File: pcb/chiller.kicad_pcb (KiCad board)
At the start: 2 copper layers, 94 x 52 mm, 43 parts, among them J1 Conn_01x03, J10 Current Sense, J11 Conn_01x14, J12 Debug, J13 Conn_01x04, J2 Conn_01x03, J3 Ext, J4 Conn_01x02, J5 Conn_01x02, J6 Conn_01x02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

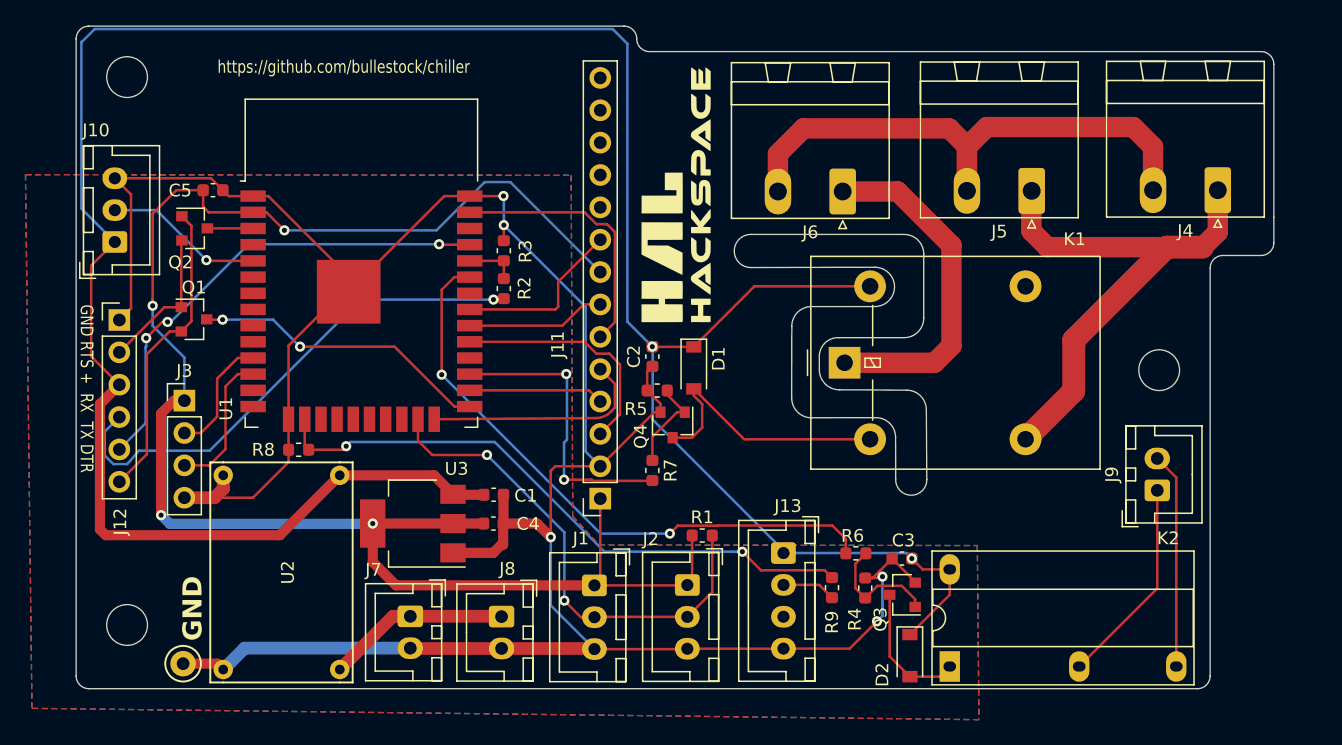
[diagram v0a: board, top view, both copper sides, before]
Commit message: Add diodes.
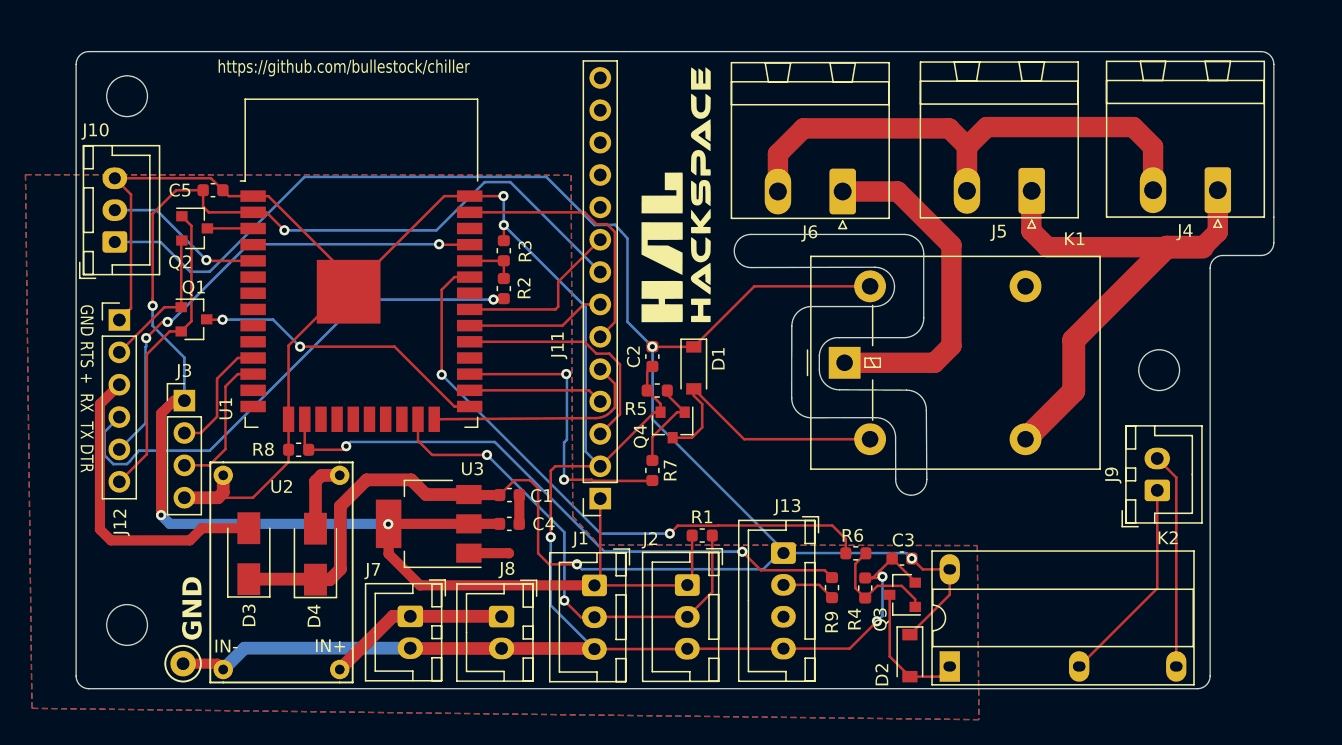
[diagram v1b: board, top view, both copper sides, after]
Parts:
- added D3: MBRA210LT3, Diode_SMD:D_SMA, F.Cu at (98.6, 114.4)
- added D4: MBRA210LT3, Diode_SMD:D_SMA, F.Cu at (103.8, 114.4)
- C1: value 1uF -> 1u
- C4: value 10uF -> 10u
- C5: value C -> 100n
- moved H1 1.50 mm to (89.0, 78.5)
- moved C4 1.24 mm to (119.0, 112.1)
- moved U3 1.24 mm to (112.7, 112.1)
- moved C1 1.24 mm to (119.0, 109.8)
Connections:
- J12 pad 3: +5V -> Net-(D3-A)
- U2 pad OUT+: +5V -> Net-(D4-A)
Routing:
- net +5V: track 202.4 -> 170.7 mm, vias 2 -> 3
- net Net-(D3-A): track 0.00 -> 24.4 mm
- net GND: track 214.1 -> 204.8 mm
- net Net-(D4-A): track 0.00 -> 5.81 mm
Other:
- board size 94 x 52 mm -> 94 x 50 mm
- board text added: "IN+"
- board text added: "IN-"

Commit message: Start adding forgotten features.
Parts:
- added J14: Flow sensor, Connector_JST:JST_XH_B3B-XH-A_1x03_P2.50mm_Vertical, F.Cu at (96.1, 78.2)
- added J15: Fan, Connector_JST:JST_XH_B2B-XH-A_1x02_P2.50mm_Vertical, F.Cu at (112.4, 78.5)
- added Q5: BSS138, Package_TO_SOT_SMD:SOT-23, F.Cu at (125.0, 79.4)
- added R10: 1k2, Resistor_SMD:R_0603_1608Metric, F.Cu at (97.9, 83.0)
- added R11: 2k2, Resistor_SMD:R_0603_1608Metric, F.Cu at (101.1, 83.0)
- J11: value Conn_01x14 -> Display; footprint Connector_PinSocket_2.54mm:PinSocket_1x14_P2.54mm_Vertical -> Connector_PinSocket_2.54mm:PinSocket_1x09_P2.54mm_Vertical
- U1: footprint RF_Module:ESP32-WROOM-32 -> RF_Module:ESP32-WROOM-32U
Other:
- board text added: "CS"
- board text added: "Fan"
- board text added: "Flow"

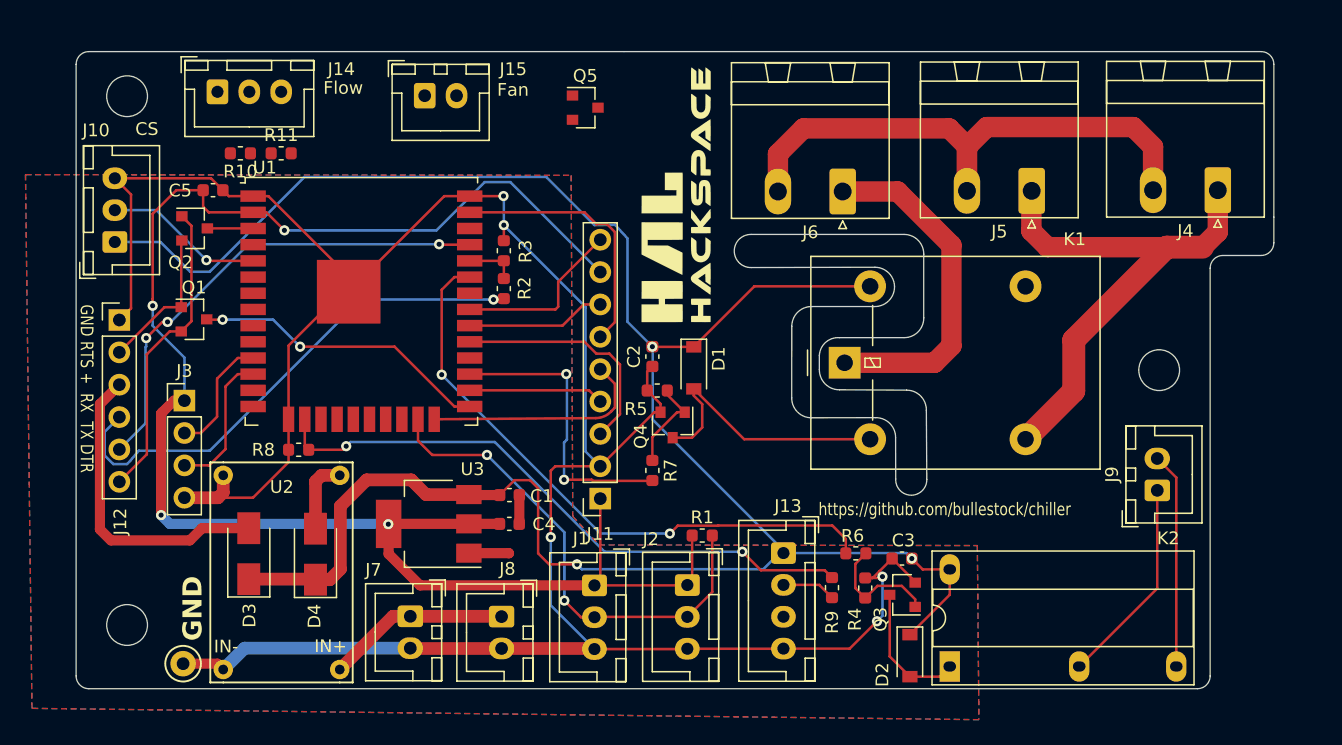
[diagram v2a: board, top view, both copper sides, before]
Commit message: Add LEDs.
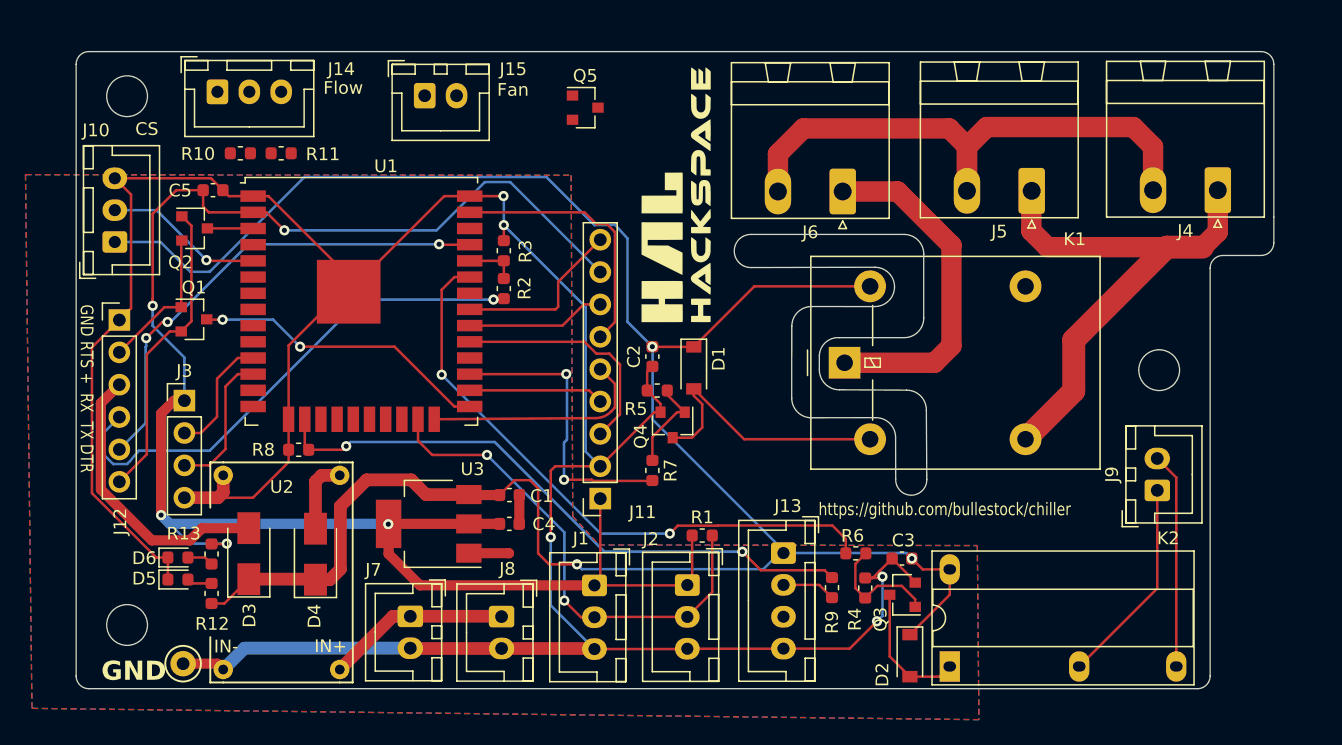
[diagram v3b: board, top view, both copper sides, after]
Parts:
- added D5: LED, LED_SMD:LED_0603_1608Metric, F.Cu at (93.0, 116.4)
- added D6: LED, LED_SMD:LED_0603_1608Metric, F.Cu at (93.0, 114.7)
- added R12: 2k7, Resistor_SMD:R_0603_1608Metric, F.Cu at (95.6, 117.5)
- added R13: 1k5, Resistor_SMD:R_0603_1608Metric, F.Cu at (95.6, 114.4)
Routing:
- net GND: track 204.8 -> 229.1 mm
- net +3V3: track 133.1 -> 140.3 mm, vias 4 -> 5
- net +5V: track 170.7 -> 174.4 mm
- net Net-(D6-A): track 0.00 -> 2.06 mm
- net Net-(D5-A): track 0.00 -> 1.98 mm
- net Net-(D3-A): track 24.4 -> 22.5 mm

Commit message: Move J9.
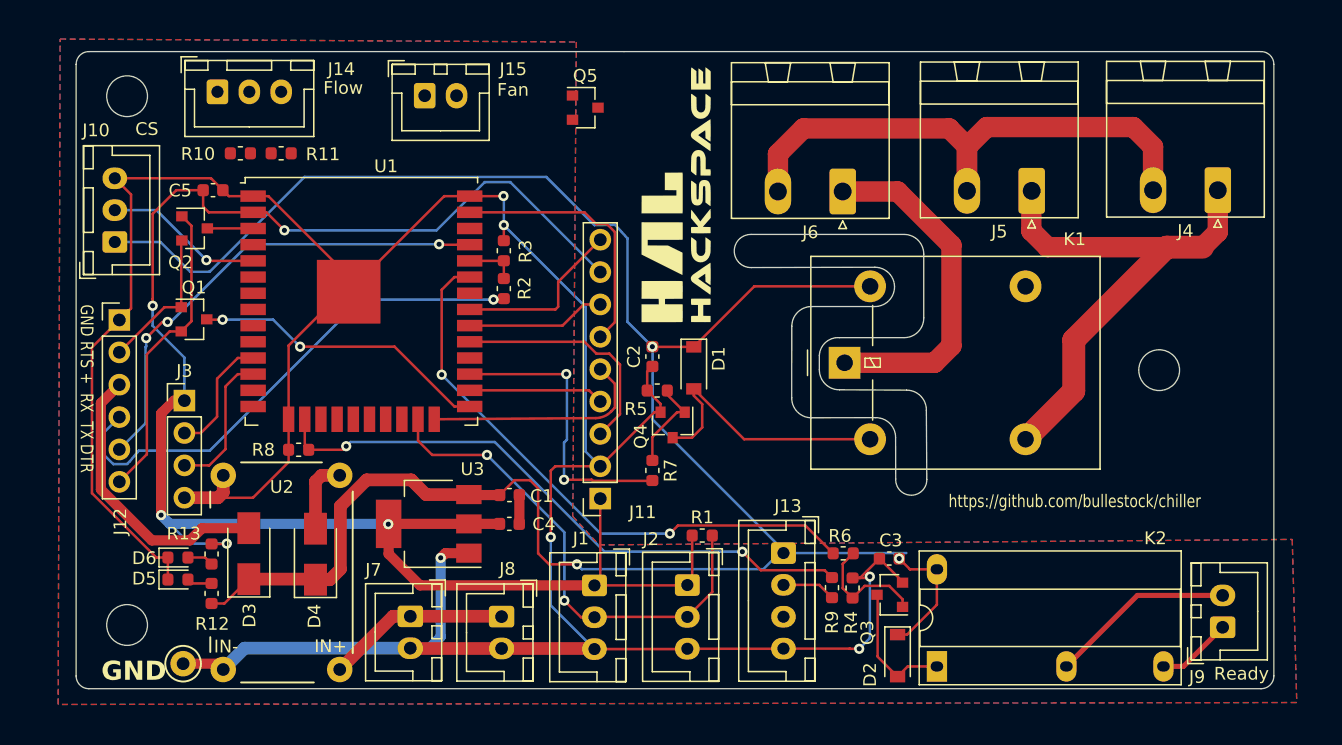
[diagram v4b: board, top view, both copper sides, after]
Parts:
- moved J9 11.9 mm to (175.0, 120.2)
- moved K2 1.01 mm to (152.6, 123.3)
- moved C3 0.99 mm to (148.8, 114.8)
- moved Q3 0.99 mm to (148.9, 117.6)
- moved R4 0.99 mm to (145.9, 117.1)
- moved R6 0.99 mm to (145.2, 114.4)
- moved D2 0.97 mm to (149.5, 122.4)
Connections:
- K2 pad 3: Net-(J9-Pin_1) -> Net-(J9-Pin_2)
- K2 pad 4: Net-(J9-Pin_2) -> Net-(J9-Pin_1)
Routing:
- net Net-(J9-Pin_1): track 16.4 -> 5.92 mm
- net GND: track 229.1 -> 237.3 mm, vias 5 -> 6
- net Net-(J9-Pin_2): track 16.9 -> 14.6 mm
- net Relay_ready: track 48.0 -> 46.3 mm
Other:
- outline, holes or cut-outs redrawn
- board text added: "Ready"

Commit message: Version 2 ready for ordering.
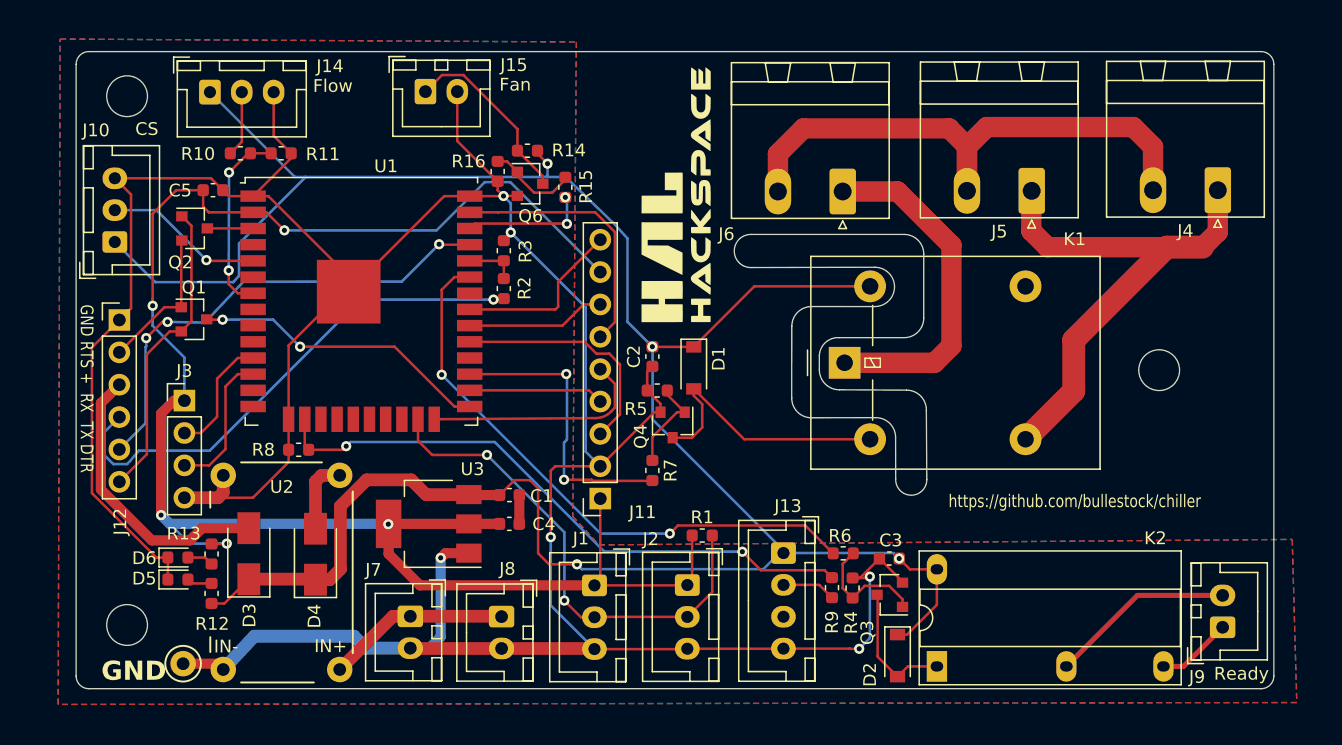
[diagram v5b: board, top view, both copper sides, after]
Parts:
- removed Q5: BSS138, Package_TO_SOT_SMD:SOT-23
- added Q6: BSS138, Package_TO_SOT_SMD:SOT-23, F.Cu at (120.6, 85.4)
- added R14: 10k, Resistor_SMD:R_0603_1608Metric, F.Cu at (120.4, 82.8)
- added R15: 1k, Resistor_SMD:R_0603_1608Metric, F.Cu at (123.4, 85.6)
- added R16: 10k, Resistor_SMD:R_0603_1608Metric, F.Cu at (118.1, 84.4)
- J1: value Conn_01x03 -> Temp sensor 1
- J2: value Conn_01x03 -> Temp sensor 2
- J4: value Conn_01x02 -> Mains in
- J5: value Conn_01x02 -> Mains out
- J6: value Conn_01x02 -> Compressor
- J7: value Conn_01x02 -> 12V in
- J8: value Conn_01x02 -> Pump
- J9: value CONN_01X02 -> Ready
- moved J14 0.59 mm to (95.5, 78.2)
- moved J15 0.33 mm to (112.4, 78.1)
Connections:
- net Net-(J7-Pin_1) renamed +12V
- J15 pad 1: unconnected-(J15-Pin_1-Pad1) -> Net-(J15-Pin_1)
- J15 pad 2: unconnected-(J15-Pin_2-Pad2) -> GND
- U1 pad 36: unconnected-(U1-IO22-Pad36) -> Fan
- U1 pad 7: unconnected-(U1-IO35-Pad7) -> Flow
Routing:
- net GND: track 237.3 -> 258.5 mm
- net Flow: track 0.00 -> 15.0 mm, vias 0 -> 2
- net Net-(J15-Pin_1): track 0.00 -> 14.6 mm
- net +5V: track 174.8 -> 188.6 mm, vias 3 -> 4
- net Fan: track 0.00 -> 9.94 mm, vias 0 -> 2
- net Net-(Q6-G): track 0.00 -> 7.13 mm
- net Net-(J14-Pin_2): track 0.00 -> 5.17 mm

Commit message: Clean up silk screen
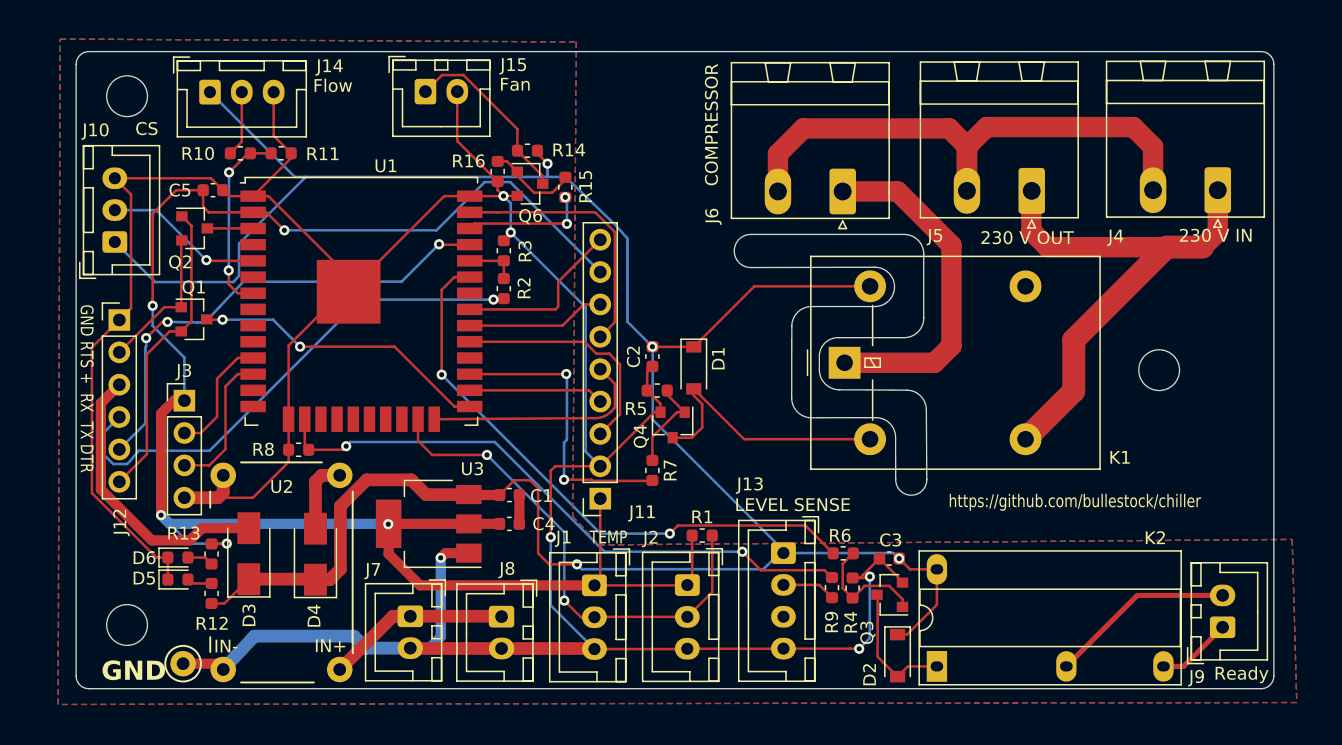
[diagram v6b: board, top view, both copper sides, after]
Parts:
- G***: moved to B.Cu
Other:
- board text added: "230 V IN"
- board text added: "230 V OUT"
- board text added: "COMPRESSOR"
- board text added: "LEVEL SENSE"
- board text added: "TEMP"
